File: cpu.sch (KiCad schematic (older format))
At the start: 11 parts, among them IC1 STM32L051K8T6, SW1 SW_PUSH

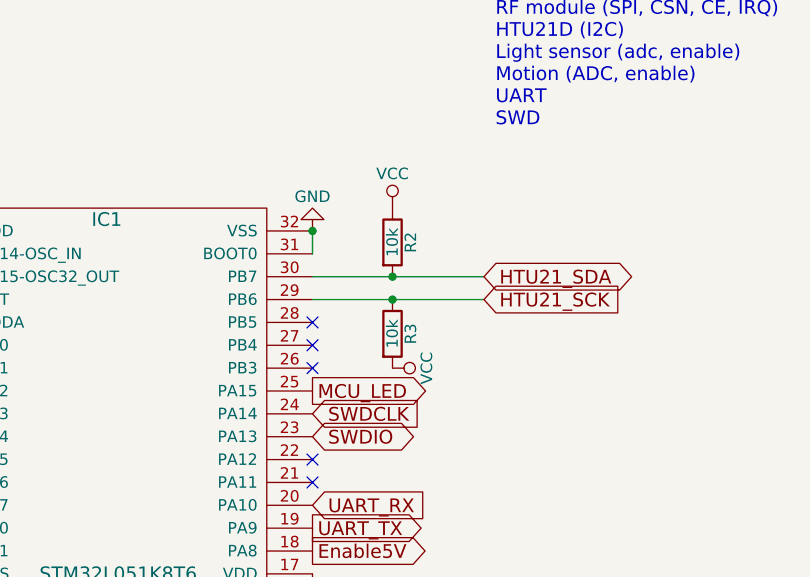
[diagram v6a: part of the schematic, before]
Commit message: Add extra switch for user defined functionality
 * reroute pcb

Signed-off-by: pluyckx <philip.luyckx@gmail.com>
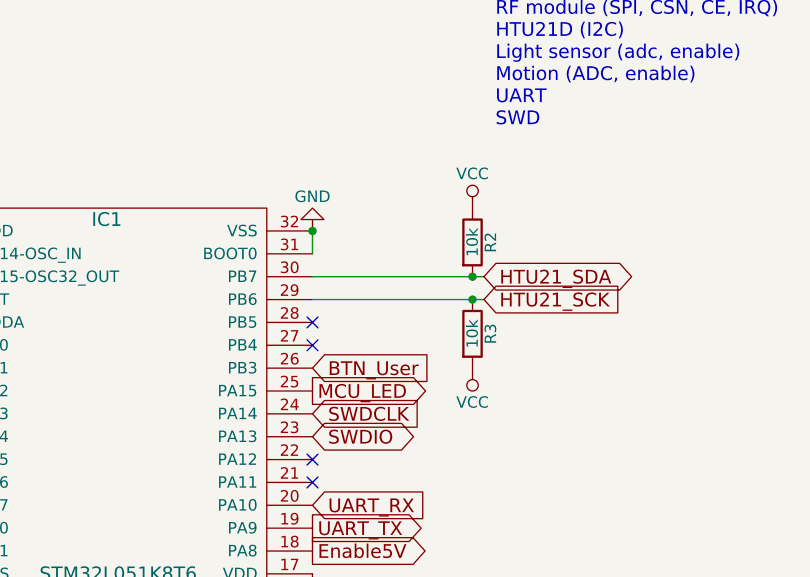
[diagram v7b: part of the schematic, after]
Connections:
- net BTN_User: now reaches IC1.26 (PB3)
- no-connect marks 8 -> 7
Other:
- moved on the sheet: R2, R3
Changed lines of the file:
@@
 NoConn ~ 7050 3600
 NoConn ~ 7050 4200
-NoConn ~ 7050 3700
 $Comp
 L STM32L051K8T6 IC1
@@
 L R R2
 U 1 1 57536ED2
-P 7400 3150
-F 0 "R2" V 7480 3150 50  0000 C CNN
-F 1 "10k" V 7400 3150 50  0000 C CNN
-F 2 "Resistors_SMD:R_0603" V 7330 3150 50  0001 C CNN
-F 3 "" H 7400 3150 50  0000 C CNN
-	1    7400 3150
+P 7750 3150
+F 0 "R2" V 7830 3150 50  0000 C CNN
+F 1 "10k" V 7750 3150 50  0000 C CNN
+F 2 "Resistors_SMD:R_0603" V 7680 3150 50  0001 C CNN
+F 3 "" H 7750 3150 50  0000 C CNN
+	1    7750 3150
 	1    0    0    -1
 $EndComp
-Connection ~ 7400 3300
+Connection ~ 7750 3300
 $Comp
 L VCC #PWR012
 U 1 1 57536F05
-P 7400 3000
-F 0 "#PWR012" H 7400 2850 50  0001 C CNN
-F 1 "VCC" H 7400 3150 50  0000 C CNN
-F 2 "" H 7400 3000 50  0000 C CNN
-F 3 "" H 7400 3000 50  0000 C CNN
-	1    7400 3000
+P 7750 3000
+F 0 "#PWR012" H 7750 2850 50  0001 C CNN
+F 1 "VCC" H 7750 3150 50  0000 C CNN
+F 2 "" H 7750 3000 50  0000 C CNN
+F 3 "" H 7750 3000 50  0000 C CNN
+	1    7750 3000
 	1    0    0    -1
 $EndComp
@@
 L R R3
 U 1 1 57536F2D
-P 7400 3550
-F 0 "R3" V 7480 3550 50  0000 C CNN
-F 1 "10k" V 7400 3550 50  0000 C CNN
-F 2 "Resistors_SMD:R_0603" V 7330 3550 50  0001 C CNN
-F 3 "" H 7400 3550 50  0000 C CNN
-	1    7400 3550
+P 7750 3550
+F 0 "R3" V 7830 3550 50  0000 C CNN
+F 1 "10k" V 7750 3550 50  0000 C CNN
+F 2 "Resistors_SMD:R_0603" V 7680 3550 50  0001 C CNN
+F 3 "" H 7750 3550 50  0000 C CNN
+	1    7750 3550
 	1    0    0    -1
 $EndComp
@@
 L VCC #PWR013
 U 1 1 57536F6A
-P 7400 3700
-F 0 "#PWR013" H 7400 3550 50  0001 C CNN
-F 1 "VCC" H 7400 3850 50  0000 C CNN
-F 2 "" H 7400 3700 50  0000 C CNN
-F 3 "" H 7400 3700 50  0000 C CNN
-	1    7400 3700
-	0    1    1    0
+P 7750 3700
+F 0 "#PWR013" H 7750 3550 50  0001 C CNN
+F 1 "VCC" H 7750 3850 50  0000 C CNN
+F 2 "" H 7750 3700 50  0000 C CNN
+F 3 "" H 7750 3700 50  0000 C CNN
+	1    7750 3700
+	-1   0    0    1
 $EndComp
-Connection ~ 7400 3400
+Connection ~ 7750 3400
 NoConn ~ 5350 3200
 NoConn ~ 7050 4100
 Text GLabel 5350 3600 0    60   Input ~ 0
 DIG_Motion
+Text GLabel 7050 3700 2    60   Input ~ 0
+BTN_User
 $EndSCHEMATC

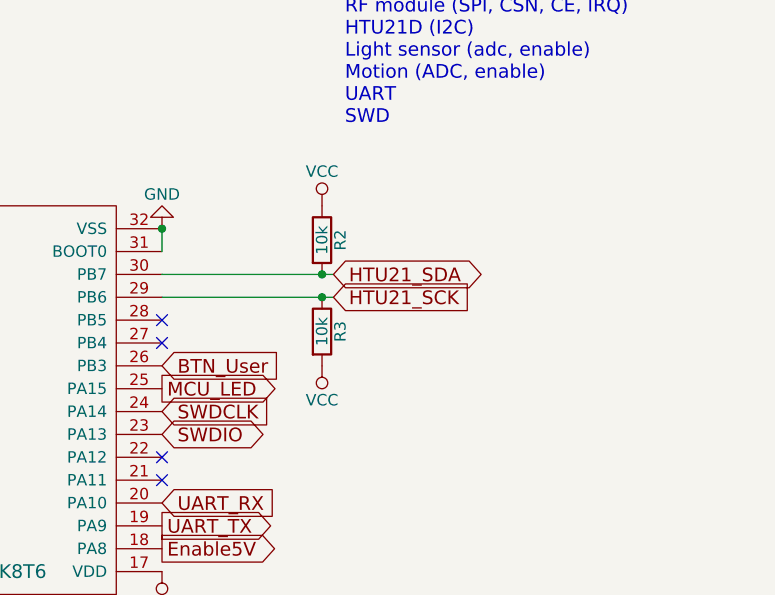
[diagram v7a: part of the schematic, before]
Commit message: Corrections I2C and Dig Opamp out
 * Fix level shift for I2C
 * Fix level shift opamp digital out (PIR)

Signed-off-by: Philip Luyckx <philip.luyckx@gmail.com>
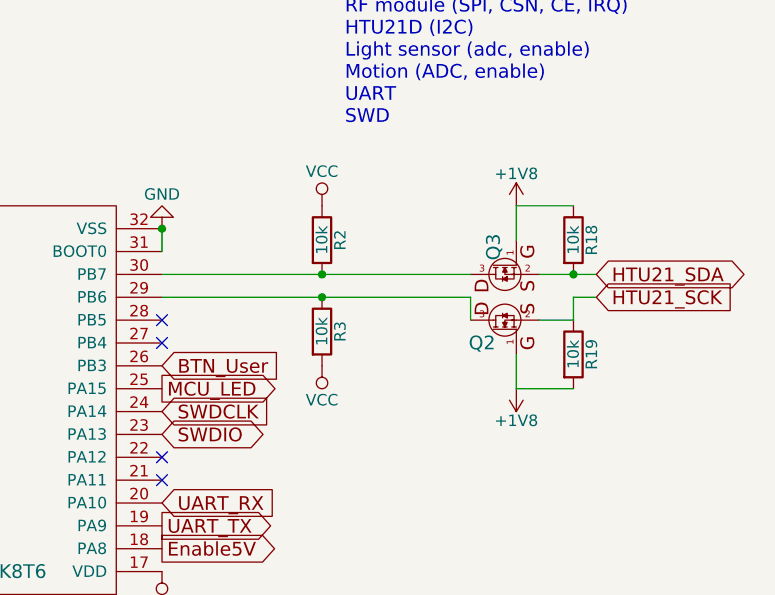
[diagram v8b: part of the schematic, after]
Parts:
- added Q2, Q3: NMosfetGen, CustomSmd:SOT23, symbol NMosfetGen
- added R18, R19: 10k, Resistors_SMD:R_0603, symbol R
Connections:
- net HTU21_SCK: now also Q3.2, R19.1; no longer IC1.29 (PB6), R3.1
- net HTU21_SDA: now also Q2.2, R18.2; no longer IC1.30 (PB7), R2.2
- new net: IC1.29 (PB6), Q3.3, R3.1
- new net: IC1.30 (PB7), Q2.3, R2.2
- new net +1V8: Q2.1, Q3.1, R18.1, R19.2
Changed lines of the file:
@@
 $EndDescr
 $Comp
-L VCC #PWR01
+L VCC #PWR1
 U 1 1 565E0F45
 P 2700 3050
-F 0 "#PWR01" H 2700 2900 50  0001 C CNN
+F 0 "#PWR1" H 2700 2900 50  0001 C CNN
 F 1 "VCC" H 2700 3200 50  0000 C CNN
 F 2 "" H 2700 3050 60  0000 C CNN
@@
 $EndComp
 $Comp
-L GND #PWR02
+L GND #PWR2
 U 1 1 565E0F59
 P 2700 3350
-F 0 "#PWR02" H 2700 3100 50  0001 C CNN
+F 0 "#PWR2" H 2700 3100 50  0001 C CNN
 F 1 "GND" H 2700 3200 50  0000 C CNN
 F 2 "" H 2700 3350 60  0000 C CNN
@@
 $EndComp
 $Comp
-L VCC #PWR03
+L VCC #PWR8
 U 1 1 565E1082
 P 5350 3100
-F 0 "#PWR03" H 5350 2950 50  0001 C CNN
+F 0 "#PWR8" H 5350 2950 50  0001 C CNN
 F 1 "VCC" H 5350 3250 50  0000 C CNN
 F 2 "" H 5350 3100 60  0000 C CNN
@@
 $EndComp
 $Comp
-L VCC #PWR04
+L VCC #PWR11
 U 1 1 565E109E
 P 7050 4600
-F 0 "#PWR04" H 7050 4450 50  0001 C CNN
+F 0 "#PWR11" H 7050 4450 50  0001 C CNN
 F 1 "VCC" H 7050 4750 50  0000 C CNN
 F 2 "" H 7050 4600 60  0000 C CNN
@@
 $EndComp
 $Comp
-L GND #PWR05
+L GND #PWR9
 U 1 1 565E10D6
 P 5350 4600
-F 0 "#PWR05" H 5350 4350 50  0001 C CNN
+F 0 "#PWR9" H 5350 4350 50  0001 C CNN
 F 1 "GND" H 5350 4450 50  0000 C CNN
 F 2 "" H 5350 4600 60  0000 C CNN
@@
 $EndComp
 $Comp
-L VCC #PWR06
+L VCC #PWR3
 U 1 1 565E12D0
 P 2700 4000
-F 0 "#PWR06" H 2700 3850 50  0001 C CNN
+F 0 "#PWR3" H 2700 3850 50  0001 C CNN
 F 1 "VCC" H 2700 4150 50  0000 C CNN
 F 2 "" H 2700 4000 60  0000 C CNN
@@
 $EndComp
 $Comp
-L GND #PWR07
+L GND #PWR4
 U 1 1 565E12F0
 P 2700 4300
-F 0 "#PWR07" H 2700 4050 50  0001 C CNN
+F 0 "#PWR4" H 2700 4050 50  0001 C CNN
 F 1 "GND" H 2700 4150 50  0000 C CNN
 F 2 "" H 2700 4300 60  0000 C CNN
@@
 $EndComp
 $Comp
-L VCC #PWR08
+L VCC #PWR5
 U 1 1 565E15CE
 P 2950 4950
-F 0 "#PWR08" H 2950 4800 50  0001 C CNN
+F 0 "#PWR5" H 2950 4800 50  0001 C CNN
 F 1 "VCC" H 2950 5100 50  0000 C CNN
 F 2 "" H 2950 4950 60  0000 C CNN
@@
 $EndComp
 $Comp
-L GND #PWR09
+L GND #PWR6
 U 1 1 565E15F4
 P 2950 6000
-F 0 "#PWR09" H 2950 5750 50  0001 C CNN
+F 0 "#PWR6" H 2950 5750 50  0001 C CNN
 F 1 "GND" H 2950 5850 50  0000 C CNN
 F 2 "" H 2950 6000 60  0000 C CNN
@@
 MCU_RST
 $Comp
-L VCC #PWR010
+L VCC #PWR7
 U 1 1 565E178E
 P 4300 3500
-F 0 "#PWR010" H 4300 3350 50  0001 C CNN
+F 0 "#PWR7" H 4300 3350 50  0001 C CNN
 F 1 "VCC" H 4300 3650 50  0000 C CNN
 F 2 "" H 4300 3500 60  0000 C CNN
@@
 Enable5V
 $Comp
-L GND #PWR011
+L GND #PWR10
 U 1 1 565E10BA
 P 7050 3100
-F 0 "#PWR011" H 7050 2850 50  0001 C CNN
+F 0 "#PWR10" H 7050 2850 50  0001 C CNN
 F 1 "GND" H 7050 2950 50  0000 C CNN
 F 2 "" H 7050 3100 60  0000 C CNN
@@
 	7050 3100 7050 3200
 NoConn ~ 5350 3300
-Text GLabel 7800 3300 2    60   BiDi ~ 0
+Text GLabel 8950 3300 2    60   BiDi ~ 0
 HTU21_SDA
-Text GLabel 7800 3400 2    60   Input ~ 0
+Text GLabel 8950 3400 2    60   Input ~ 0
 HTU21_SCK
 Wire Wire Line
-	7050 3300 7800 3300
-Wire Wire Line
-	7800 3400 7050 3400
+	7050 3300 8400 3300
+Wire Wire Line
+	7050 3400 8400 3400
 $Comp
 L R R2
@@
 Connection ~ 7750 3300
 $Comp
-L VCC #PWR012
+L VCC #PWR12
 U 1 1 57536F05
 P 7750 3000
-F 0 "#PWR012" H 7750 2850 50  0001 C CNN
+F 0 "#PWR12" H 7750 2850 50  0001 C CNN
 F 1 "VCC" H 7750 3150 50  0000 C CNN
 F 2 "" H 7750 3000 50  0000 C CNN
@@
 $EndComp
 $Comp
-L VCC #PWR013
+L VCC #PWR13
 U 1 1 57536F6A
 P 7750 3700
-F 0 "#PWR013" H 7750 3550 50  0001 C CNN
+F 0 "#PWR13" H 7750 3550 50  0001 C CNN
 F 1 "VCC" H 7750 3850 50  0000 C CNN
 F 2 "" H 7750 3700 50  0000 C CNN
@@
 Text GLabel 7050 3700 2    60   Input ~ 0
 BTN_User
+$Comp
+L NMosfetGen Q2
+U 1 1 586E95AA
+P 8550 3300
+F 0 "Q2" V 8850 3400 60  0000 C CNN
+F 1 "NMosfetGen" V 8300 3550 60  0001 C CNN
+F 2 "CustomSmd:SOT23" H 8500 3440 60  0001 C CNN
+F 3 "" H 8500 3440 60  0000 C CNN
+	1    8550 3300
+	0    -1   1    0
+$EndComp
+Wire Wire Line
+	8700 3300 8950 3300
+$Comp
+L +1V8 #PWR14
+U 1 1 586E9891
+P 8600 3000
+F 0 "#PWR14" H 8600 2850 50  0001 C CNN
+F 1 "+1V8" H 8600 3140 50  0000 C CNN
+F 2 "" H 8600 3000 50  0000 C CNN
+F 3 "" H 8600 3000 50  0000 C CNN
+	1    8600 3000
+	1    0    0    -1
+$EndComp
+$Comp
+L R R18
+U 1 1 586E98C9
+P 8850 3150
+F 0 "R18" V 8930 3150 50  0000 C CNN
+F 1 "10k" V 8850 3150 50  0000 C CNN
+F 2 "Resistors_SMD:R_0603" V 8780 3150 50  0001 C CNN
+F 3 "" H 8850 3150 50  0000 C CNN
+	1    8850 3150
+	1    0    0    -1
+$EndComp
+Connection ~ 8850 3300
+Wire Wire Line
+	8600 3000 8850 3000
+Wire Wire Line
+	8600 3000 8600 3150
+$Comp
+L NMosfetGen Q3
+U 1 1 586E9A1D
+P 8550 3500
+F 0 "Q3" H 8870 3550 60  0000 C CNN
+F 1 "NMosfetGen" V 8350 3750 60  0001 C CNN
+F 2 "CustomSmd:SOT23" H 8500 3640 60  0001 C CNN
+F 3 "" H 8500 3640 60  0000 C CNN
+	1    8550 3500
+	0    -1   -1   0
+$EndComp
+Wire Wire Line
+	8400 3400 8400 3500
+Wire Wire Line
+	8700 3500 8850 3500
+Wire Wire Line
+	8850 3500 8850 3400
+Wire Wire Line
+	8850 3400 8950 3400
+$Comp
+L R R19
+U 1 1 586E9B76
+P 8850 3650
+F 0 "R19" V 8930 3650 50  0000 C CNN
+F 1 "10k" V 8850 3650 50  0000 C CNN
+F 2 "Resistors_SMD:R_0603" V 8780 3650 50  0001 C CNN
+F 3 "" H 8850 3650 50  0000 C CNN
+	1    8850 3650
+	1    0    0    -1
+$EndComp
+Wire Wire Line
+	8850 3800 8600 3800
+Wire Wire Line
+	8600 3800 8600 3650
+$Comp
+L +1V8 #PWR15
+U 1 1 586E9BE5
+P 8600 3800
+F 0 "#PWR15" H 8600 3650 50  0001 C CNN
+F 1 "+1V8" H 8600 3940 50  0000 C CNN
+F 2 "" H 8600 3800 50  0000 C CNN
+F 3 "" H 8600 3800 50  0000 C CNN
+	1    8600 3800
+	-1   0    0    1
+$EndComp
 $EndSCHEMATC
